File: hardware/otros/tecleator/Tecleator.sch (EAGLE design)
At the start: 53 parts, among them T1 BC547

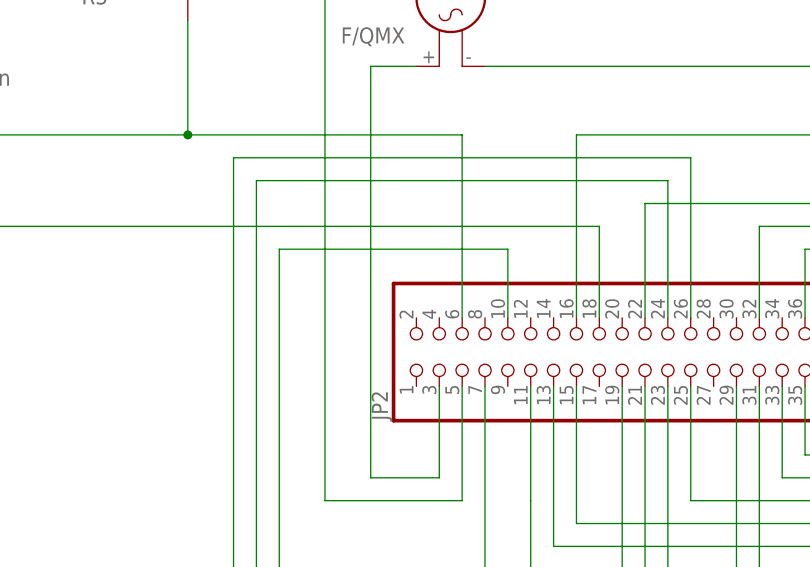
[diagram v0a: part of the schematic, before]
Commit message: 
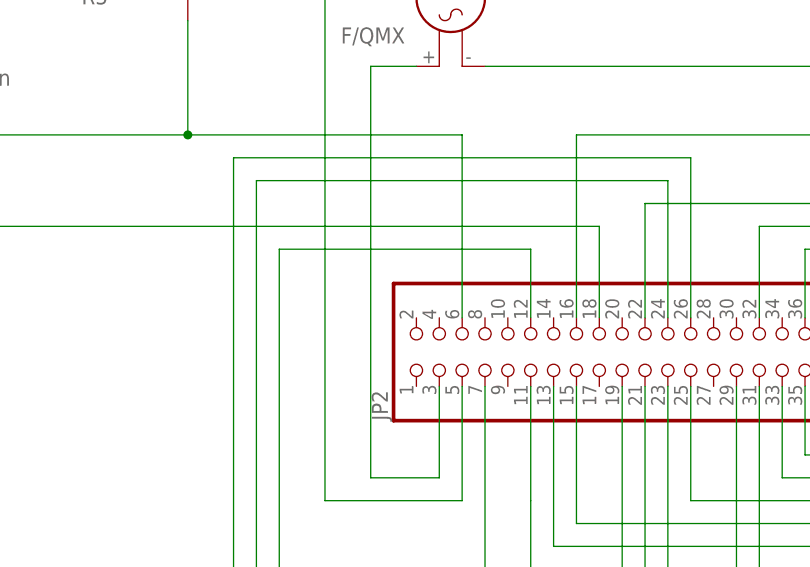
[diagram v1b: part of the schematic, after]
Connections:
- net VET: now also JP2.12; no longer JP2.10
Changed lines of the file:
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@@
 <junction x="106.68" y="40.64"/>
 <wire x1="-38.1" y1="101.6" x2="114.3" y2="101.6" width="0.1524" layer="91"/>
-<pinref part="JP2" gate="A" pin="10"/>
-<wire x1="-12.7" y1="132.08" x2="-12.7" y2="139.7" width="0.1524" layer="91"/>
-<wire x1="-12.7" y1="139.7" x2="-38.1" y2="139.7" width="0.1524" layer="91"/>
+<wire x1="-10.16" y1="139.7" x2="-38.1" y2="139.7" width="0.1524" layer="91"/>
 <wire x1="-38.1" y1="139.7" x2="-38.1" y2="101.6" width="0.1524" layer="91"/>
+<pinref part="JP2" gate="A" pin="12"/>
+<wire x1="-10.16" y1="139.7" x2="-10.16" y2="132.08" width="0.1524" layer="91"/>
 </segment>
 </net>
